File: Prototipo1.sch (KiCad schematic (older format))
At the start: 41 parts

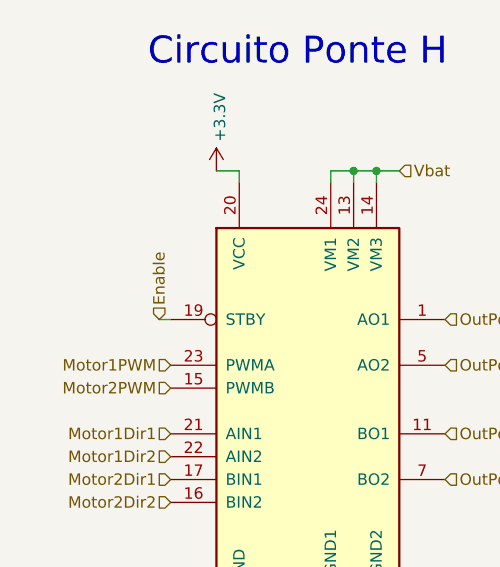
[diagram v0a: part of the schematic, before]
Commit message: Adicionado resistor de pull down na ponte H
Adicionado resistor de pull down no pino enable da ponte H
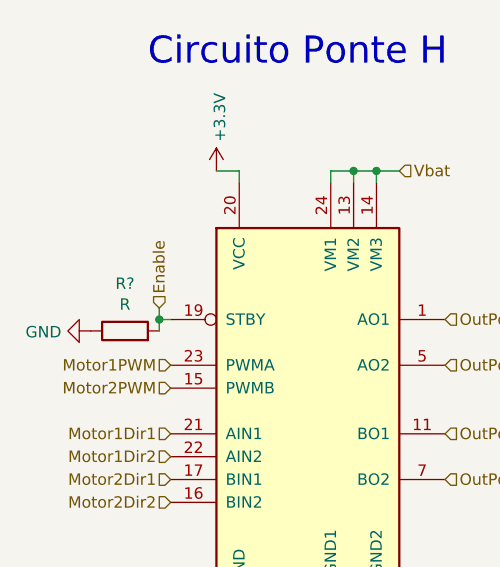
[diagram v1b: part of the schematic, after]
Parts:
- added R?: R, symbol Device:R
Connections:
- net Enable: now also R?.2
- net GND: now also R?.1
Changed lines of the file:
@@
-$Comp
-L Device:C C?
-U 1 1 5F02A3CB
-P 10350 5500
-F 0 "C?" H 10200 5600 50  0000 L CNN
-F 1 "C" H 10200 5400 50  0000 L CNN
-F 2 "" H 10388 5350 50  0001 C CNN
-F 3 "~" H 10350 5500 50  0001 C CNN
-	1    10350 5500
-	1    0    0    -1
-$EndComp
 $Comp
 L Device:C C?
@@
 Wire Wire Line
 	10350 5950 10650 5950
-Wire Wire Line
-	10350 5750 10350 5650
 Connection ~ 10350 5750
 Wire Wire Line
 	10350 5750 10650 5750
-Wire Wire Line
-	10350 5350 10350 5250
 Connection ~ 10350 5250
 Wire Wire Line
@@
 Wire Wire Line
 	1150 6350 1500 6350
-Text HLabel 950  2100 1    50   Input ~ 0
+Text HLabel 950  2050 1    50   Input ~ 0
 Enable
 Text HLabel 7400 2000 0    50   Input ~ 0
@@
 	2200 6350 2550 6350
 Connection ~ 2200 6350
-Text HLabel 1150 7250 3    50   Input ~ 0
-PortaDigital1
-Text HLabel 1500 7250 3    50   Input ~ 0
-PortaDigital2
 Text HLabel 1850 7250 3    50   Input ~ 0
 PortaDigital3
@@
 	0    -1   -1   0
 $EndComp
+Wire Wire Line
+	950  2150 950  2100
+Wire Wire Line
+	950  2100 950  2050
+Connection ~ 950  2100
+$Comp
+L power:GND #PWR?
+U 1 1 5F574261
+P 650 2150
+F 0 "#PWR?" H 650 1900 50  0001 C CNN
+F 1 "GND" V 655 2022 50  0000 R CNN
+F 2 "" H 650 2150 50  0001 C CNN
+F 3 "" H 650 2150 50  0001 C CNN
+	1    650  2150
+	0    1    1    0
+$EndComp
+Text HLabel 1500 7250 3    50   Input ~ 0
+PortaDigital2
+Text HLabel 1150 7250 3    50   Input ~ 0
+PortaDigital1
+Wire Wire Line
+	10350 5350 10350 5250
+Wire Wire Line
+	10350 5750 10350 5650
+$Comp
+L Device:C C?
+U 1 1 5F02A3CB
+P 10350 5500
+F 0 "C?" H 10200 5600 50  0000 L CNN
+F 1 "C" H 10200 5400 50  0000 L CNN
+F 2 "" H 10388 5350 50  0001 C CNN
+F 3 "~" H 10350 5500 50  0001 C CNN
+	1    10350 5500
+	1    0    0    -1
+$EndComp
+$Comp
+L Device:R R?
+U 1 1 5F55E191
+P 800 2150
+F 0 "R?" V 1007 2150 50  0000 C CNN
+F 1 "R" V 916 2150 50  0000 C CNN
+F 2 "" V 730 2150 50  0001 C CNN
+F 3 "~" H 800 2150 50  0001 C CNN
+	1    800  2150
+	0    -1   -1   0
+$EndComp

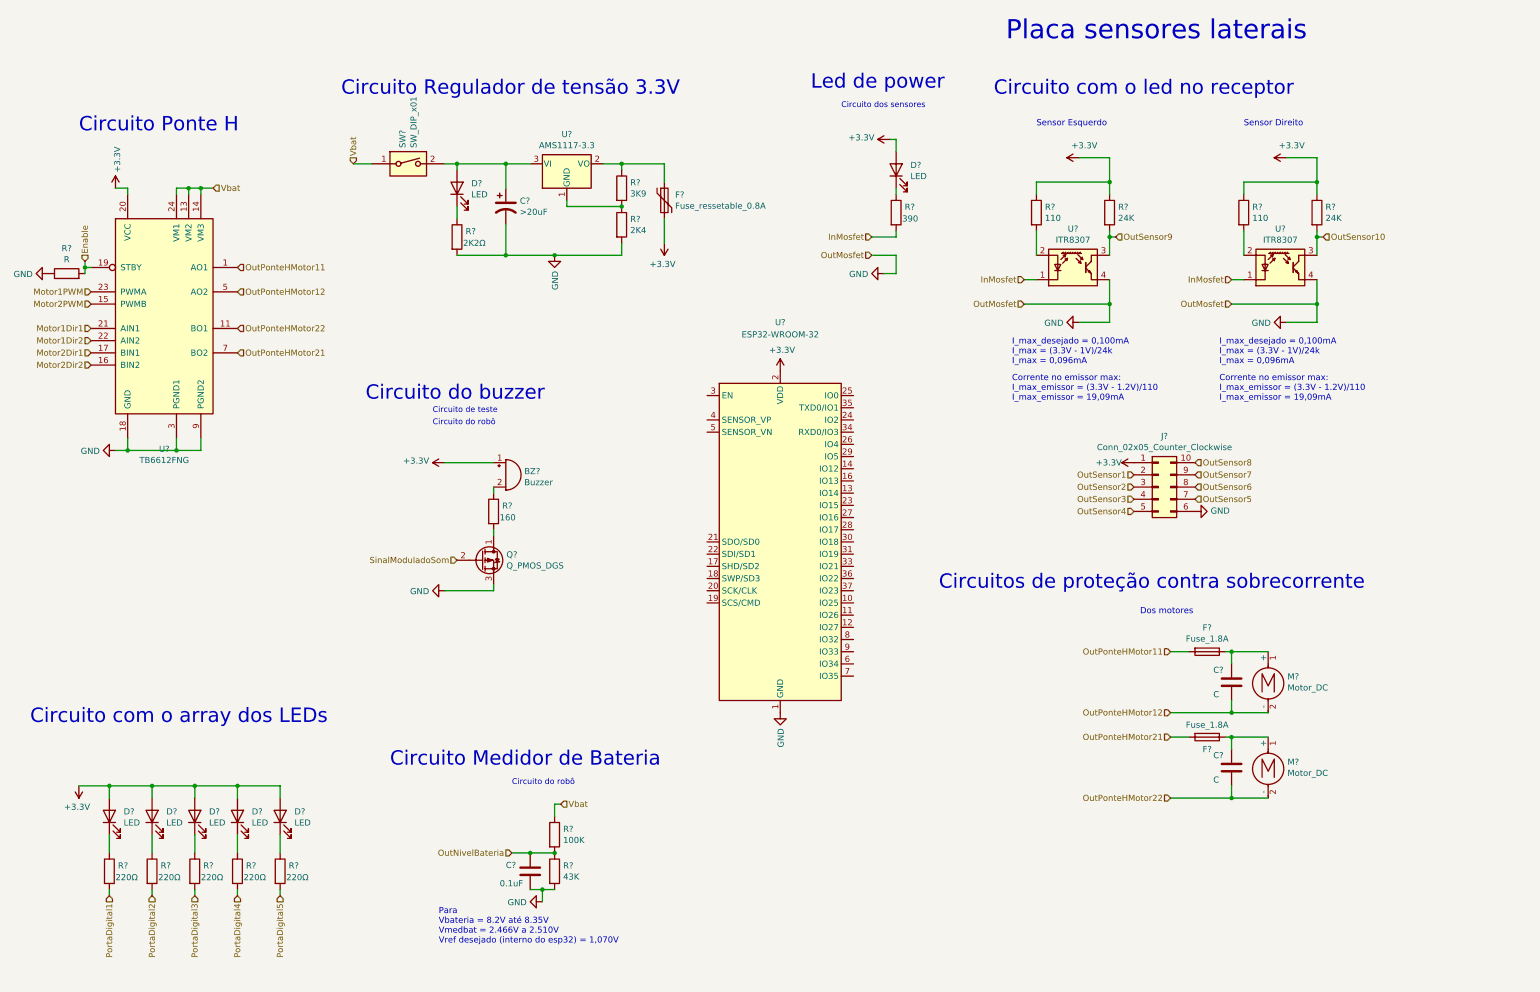
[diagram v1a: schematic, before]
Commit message: Criação inicial do arquivo de PCI e atualização de esquemático
Criação de um projeto de PCI não finalizado e incompleto, como demonstração de um curso com a Gabrielly. Atualizado o esquemático da ponte H e associado alguns componentes.
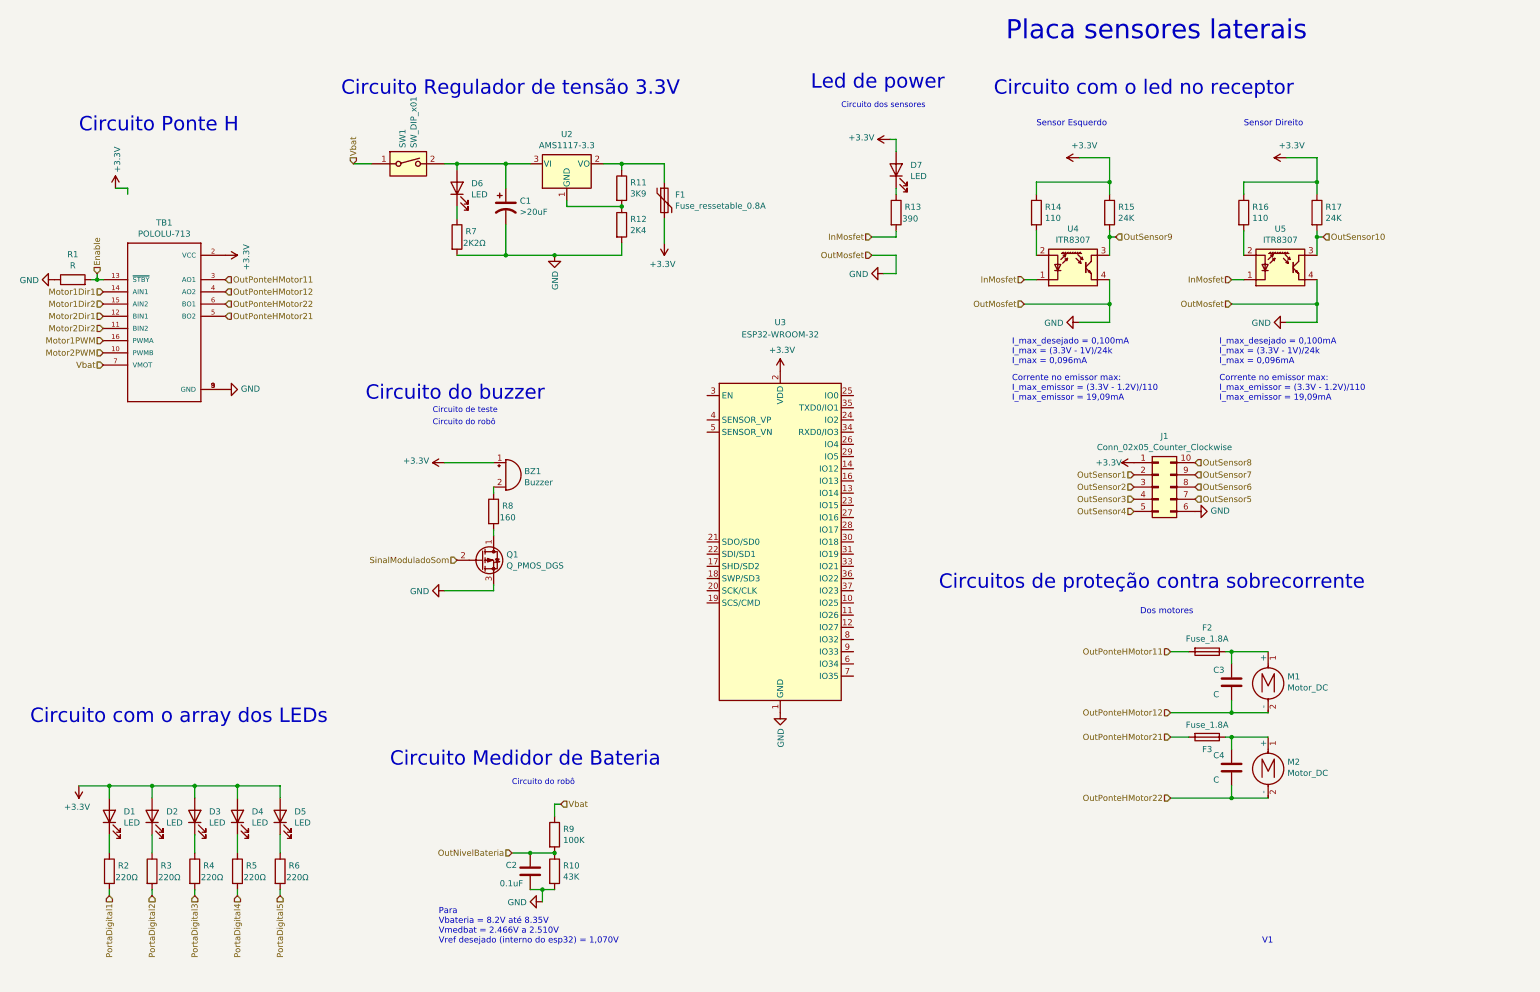
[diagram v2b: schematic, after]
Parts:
- removed U?: TB6612FNG, Package_SO:SSOP-24_5.3x8.2mm_P0.65mm, symbol Driver_Motor:TB6612FNG
- added TB1: POLOLU-713, POLOLU-713:SHIELD_POLOLU-713, symbol POLOLU-713:POLOLU-713
- BZ1: renamed from BZ?; footprint (none) -> Buzzer_Beeper:Buzzer_12x9.5RM7.6
- J1: renamed from J?; footprint (none) -> Connector_IDC:IDC-Header_2x05_P2.54mm_Vertical
- M1, M2: renamed from M?; footprint (none) -> TerminalBlock:TerminalBlock_bornier-2_P5.08mm
- Q1: renamed from Q?; footprint (none) -> Package_TO_SOT_SMD:SOT-23
- R10, R2, R3, R4, R5, R6, R7, R8, R9: renamed from R?; footprint (none) -> Resistor_SMD:R_0805_2012Metric_Pad1.15x1.40mm_HandSolder
- SW1: renamed from SW?; footprint (none) -> Button_Switch_SMD:SW_DIP_SPSTx01_Slide_9.78x4.72mm_W8.61mm_P2.54mm
- gave numbers to parts that had none: 26
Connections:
- net +3V3: now also TB1.2 (VCC)
- net Enable: now also TB1.13 (~STBY~)
- net GND: now also TB1.1 (GND), TB1.8 (GND), TB1.9 (GND)
- net Motor1Dir1: now also TB1.14 (AIN1)
- net Motor1Dir2: now also TB1.15 (AIN2)
- net Motor1PWM: now also TB1.16 (PWMA)
- net Motor2Dir1: now also TB1.12 (BIN1)
- net Motor2Dir2: now also TB1.11 (BIN2)
- net Motor2PWM: now also TB1.10 (PWMB)
- net OutPonteHMotor11: now also TB1.3 (AO1)
- net OutPonteHMotor12: now also TB1.4 (AO2)
- net OutPonteHMotor21: now also TB1.5 (BO2)
- net OutPonteHMotor22: now also TB1.6 (BO1)
- net Vbat: now also TB1.7 (VMOT)
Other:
- note added: "V1"
- moved on the sheet: R1
